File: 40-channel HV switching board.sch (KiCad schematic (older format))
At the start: 0 parts

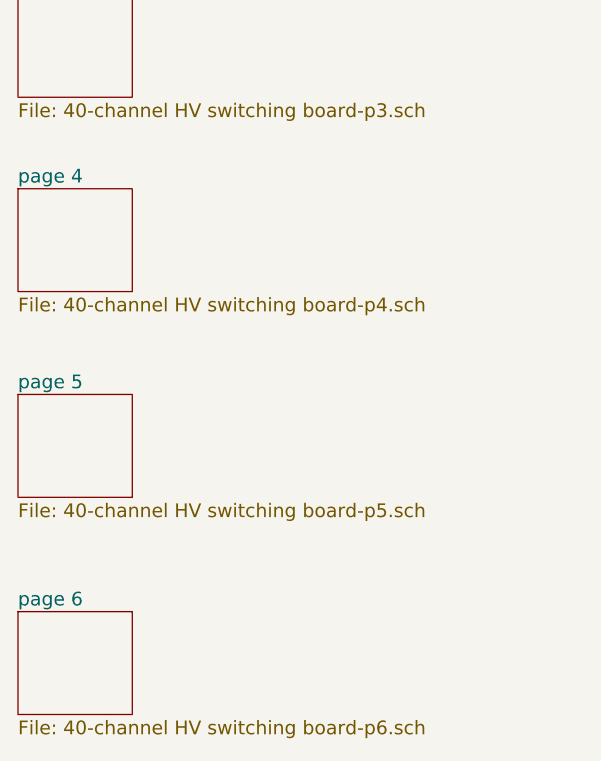
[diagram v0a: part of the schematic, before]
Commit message: Reroute onto 2-layer board, remove inverters
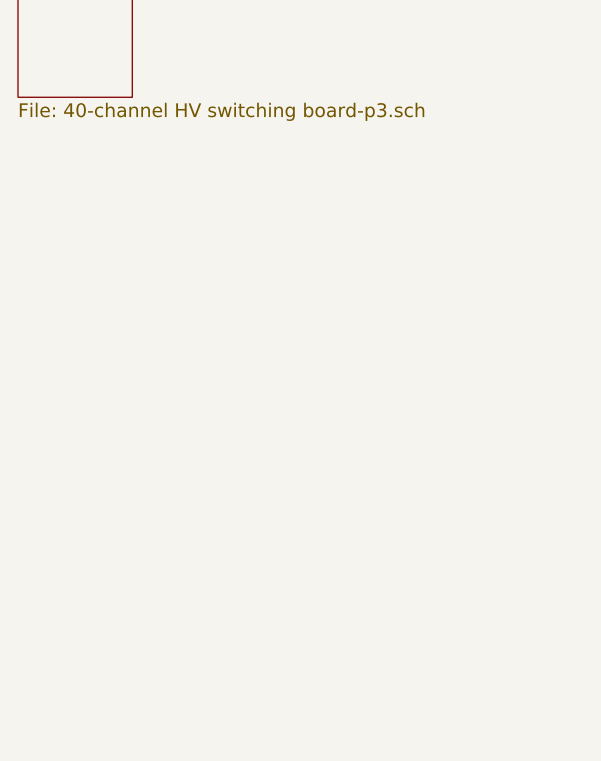
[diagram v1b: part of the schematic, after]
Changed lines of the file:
@@
 $Descr User 11000 8500
 encoding utf-8
-Sheet 1 7
+Sheet 1 4
 Title "40-channel HV switching board"
-Date "11 sep 2013"
+Date "28 jan 2014"
 Rev "1"
 Comp "Ryan Fobel"
@@
 F1 "40-channel HV switching board-p3.sch" 60
 $EndSheet
-$Sheet
-S 1050 3350 500  450
-U 4E3312C1
-F0 "page 4" 60
-F1 "40-channel HV switching board-p4.sch" 60
-$EndSheet
-$Sheet
-S 1050 4250 500  450
-U 4E33135C
-F0 "page 5" 60
-F1 "40-channel HV switching board-p5.sch" 60
-$EndSheet
-$Sheet
-S 1050 5200 500  450
-U 4E33141F
-F0 "page 6" 60
-F1 "40-channel HV switching board-p6.sch" 60
-$EndSheet
 $EndSCHEMATC

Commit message: Fix BOM, labels, reorganize schematic
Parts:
- added C1, C12, C13, C14, C3, C5, C6, C8, C9: 0.1uF, symbol C
- added C10, C11: 22pF, symbol C
- added C2, C4: 33uF, symbol CP1
- added C7: 0.01uF, symbol C
- added DS1: +5V, symbol LED
- added DS2: VCC, symbol LED
- added DS3: PROG_MODE, symbol LED
- added DS4: RST, symbol LED
- added IC1: ATMEG328PU, DIL28, symbol ATMEGA8-P
- added J1: CONN_4, symbol CONN_4
- added J2: CONN_10, symbol CONN_10
- added J3, J4: CONN_2, symbol CONN_2
- added J5: CONN_40, symbol CONN_40
- added JP1, JP2: JUMPER, ~, symbol JUMPER
- added JP3: ISP RESET, ~, symbol JUMPER
- added P1, P2: CONN_6, symbol CONN_6
- added R100, R125, R126, R127, R45: 1k, symbol R
- added R43: 10k, symbol R
- added R99: 1Meg, symbol R
- added SW1: DPST, symbol DPST
- added U1, U2, U3, U4, U5: 74HC595A, ~, symbol 74HC595A
- added U6: 7400, ~, symbol 7400
- added X1: 16MHz, ~, symbol CRYSTAL
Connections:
- net labels added: +5V, +5V_USB, A4/SDA, A5/SCL, D10/SS, D11/MOSI, D12/MISO, D13/SCK, D3/S_SS, D4/S_SCK, D5/S_MOSI, D7, D8/OE, D9/SRCLR, GND, HV, HVGND, HVOUT0, HVOUT1, HVOUT10, HVOUT11, HVOUT12, HVOUT13, HVOUT14, HVOUT15, HVOUT16, HVOUT17, HVOUT18, HVOUT19, HVOUT2, HVOUT20, HVOUT21, HVOUT22, HVOUT23, HVOUT24, HVOUT25, HVOUT26, HVOUT27, HVOUT28, HVOUT29, HVOUT3, HVOUT30, HVOUT31, HVOUT32, HVOUT33, HVOUT34, HVOUT35, HVOUT36, HVOUT37, HVOUT38, HVOUT39, HVOUT4, HVOUT5, HVOUT6, HVOUT7, HVOUT8, HVOUT9, OUT0, OUT1, OUT10, OUT11, OUT12, OUT13, OUT14, OUT15, OUT16, OUT17, OUT18, OUT19, OUT2, OUT20, OUT21, OUT22, OUT23, OUT24, OUT25, OUT26, OUT27, OUT28, OUT29, OUT3, OUT30, OUT31, OUT32, OUT33, OUT34, OUT35, OUT36, OUT37, OUT38, OUT39, OUT4, OUT5, OUT6, OUT7, OUT8, OUT9, RST, RX, TX, VCC
- wire segments 0 -> 65
- no-connect marks 0 -> 11
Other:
- note added: "ARDUINO PROGRAMMING INTERFACE"
- note added: "COMMUNICATION\nBUS"
- note added: "FROM\nHV AMPLIFIER"
- note added: "ISP"
- note added: "ISP LATCH"
- note added: "PASS THROUGH\nTO NEXT BOARD"
- note added: "POWER"
- note added: "POWER JUMPERS"
- note added: "SHIFT REGISTERS"
- note added: "SWITCHES"
- note added: "TO DMF CHIP"

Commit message: Update for compatibility with KiCad 4.0
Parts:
- removed J1: CONN_4, symbol CONN_4
- removed J2: CONN_10, symbol CONN_10
- removed J3, J4: CONN_2, symbol CONN_2
- removed J5: CONN_40, symbol CONN_40
- removed P1, P2: CONN_6, symbol CONN_6
- removed SW1: DPST, symbol DPST
- added J1: CONN_01X04, symbol CONN_01X04
- added J2: CONN_01X10, symbol CONN_01X10
- added J3, J4: BNC, symbol BNC
- added J5: CONN_01X40, symbol CONN_01X40
- added P1, P2: CONN_01X06, symbol CONN_01X06
- added SW1: Switch_DPST, symbol Switch_DPST
- IC1: footprint DIL28 -> (none)
- JP1, JP2, JP3, U1, U2, U3, U4, U5, U6: footprint ~ -> (none)
- X1: footprint ~ -> (none); symbol CRYSTAL -> Crystal
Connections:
- wire segments 65 -> 88

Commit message: Update to work with KiCad 4.0
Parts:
- C1, C10, C11, C12, C13, C14, C3, C5, C6, C7, C8, C9: footprint (none) -> Capacitors_SMD:C_1206
- C2, C4: footprint (none) -> footprints:SM2917
- DS1, DS2, DS3, DS4: footprint (none) -> LEDs:LED_1206
- IC1: footprint (none) -> Housings_DIP:DIP-28_W7.62mm
- J1: footprint (none) -> footprints:Molex_15-24-4441
- J2: footprint (none) -> Connect:HE10-10C
- J3, J4: footprint (none) -> footprints:JACK_SMA
- J5: footprint (none) -> footprints:TFML-120-01-XXX-D-RA
- JP1, JP2, JP3: footprint (none) -> Pin_Headers:Pin_Header_Straight_1x02
- P1: footprint (none) -> Pin_Headers:Pin_Header_Angled_1x06
- P2: footprint (none) -> Pin_Headers:Pin_Header_Straight_2x03
- R100, R125, R126, R127, R43, R45, R99: footprint (none) -> Resistors_SMD:R_1206
- SW1: footprint (none) -> footprints:SW_PUSH_6mm
- U1, U2, U3, U4, U5: footprint (none) -> footprints:SO16E
- U6: footprint (none) -> footprints:SO14E
- X1: footprint (none) -> Crystals:HC-49V
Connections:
- wire segments 88 -> 89
